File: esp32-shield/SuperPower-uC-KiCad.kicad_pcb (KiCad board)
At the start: 4 copper layers, 45.1 x 45.1 mm, 29 parts, among them J11 DNP, J5 Conn_01x14_Female, J6 Conn_01x14_Female, J9 MCU board, Q3 S8050, Q4 S8050, SW1 DNP, U13 ESP32-WROOM32, U14 W25Q32JVSS, U5 CH340G, U6 AMS1117-3.3, Y1 12MHZ

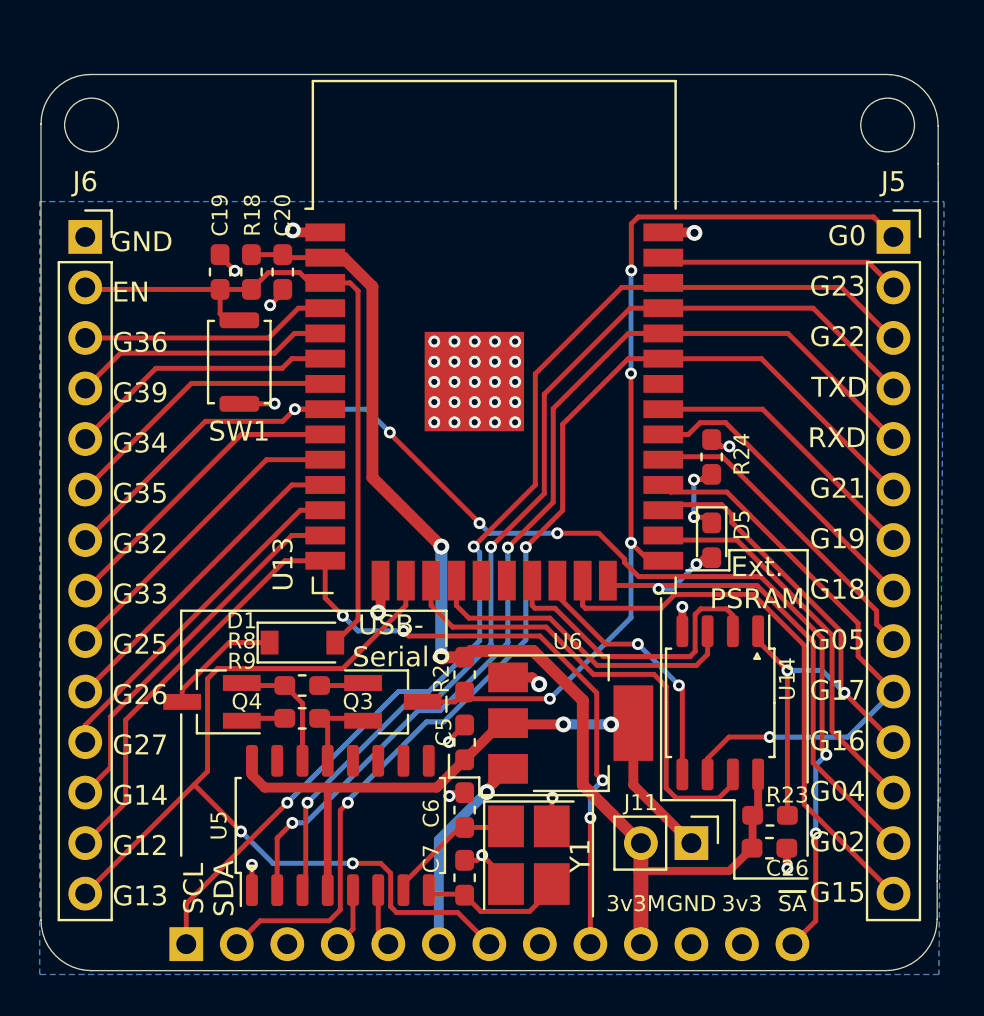
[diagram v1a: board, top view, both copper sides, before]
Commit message: added rgbw led, swapped ch340g for ch340c part numers
also marked crystal and caps as DNP
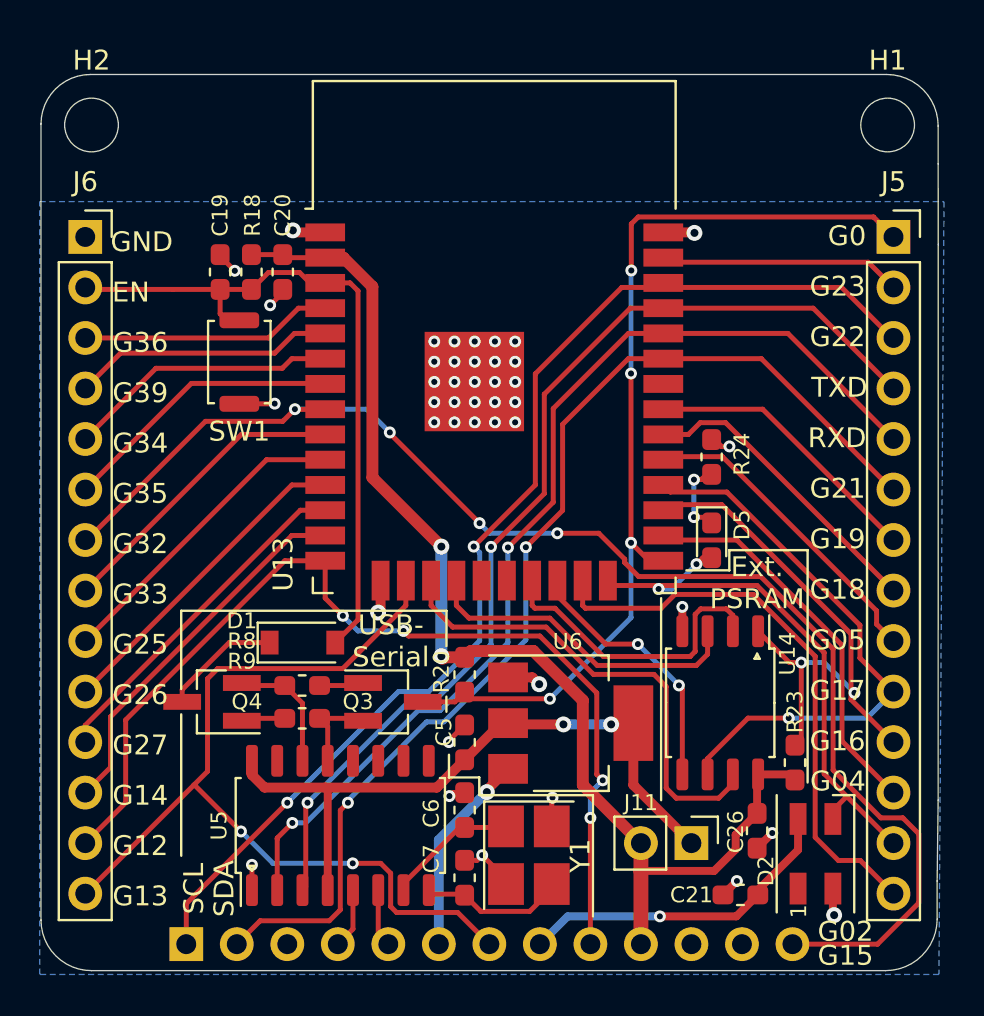
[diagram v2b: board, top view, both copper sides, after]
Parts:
- removed H4: MountingHole, MountingHole:MountingHole_2.7mm_M2.5_ISO7380
- added C21: 0.1µF, Capacitor_SMD:C_0603_1608Metric_Pad1.05x0.95mm_HandSolder, F.Cu at (161.1, 114.6)
- added D2: SK6812MINI, LED_SMD:LED_SK6812MINI_PLCC4_3.5x3.5mm_P1.75mm, F.Cu at (164.8, 112.5)
- added H1: MountingHole, MountingHole:MountingHole_2.7mm_M2.5_ISO7380, F.Cu at (168.5, 75.9)
- U5: value CH340G -> CH340C
- moved R23 2.94 mm to (163.8, 108.0), turned to 90 degrees
- moved C26 1.07 mm to (161.9, 111.4), turned to 90 degrees
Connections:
- net /3v3_MCU_2 renamed /3v3_MCU
- net /D2+ renamed /D+
- net /D2- renamed /D-
- net /SCL_2 renamed /SCL
- net /SDA_2 renamed /SDA
- net /VBUS_2 renamed /VBUS
- J9 pad 8: Net-(J9-Pad8) -> /5V
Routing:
- net /5V: track 0.00 -> 16.6 mm, vias 0 -> 1
- net /~SMBALERT: track 62.4 -> 69.4 mm, vias 6 -> 4
- net /MCU Module/IO16: track 31.8 -> 29.0 mm
- net GND: track 21.6 -> 23.9 mm, vias 40 -> 42
- net /3v3_MCU: track 58.5 -> 60.1 mm
- net /MCU Module/IO2: track 27.3 -> 28.7 mm
- net /MCU Module/IO15: track 28.1 -> 28.8 mm
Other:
- copper layers 4 -> 2
- board text removed: "3v3M"
- board text removed: "~SA"

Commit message: added more input caps & part number for button
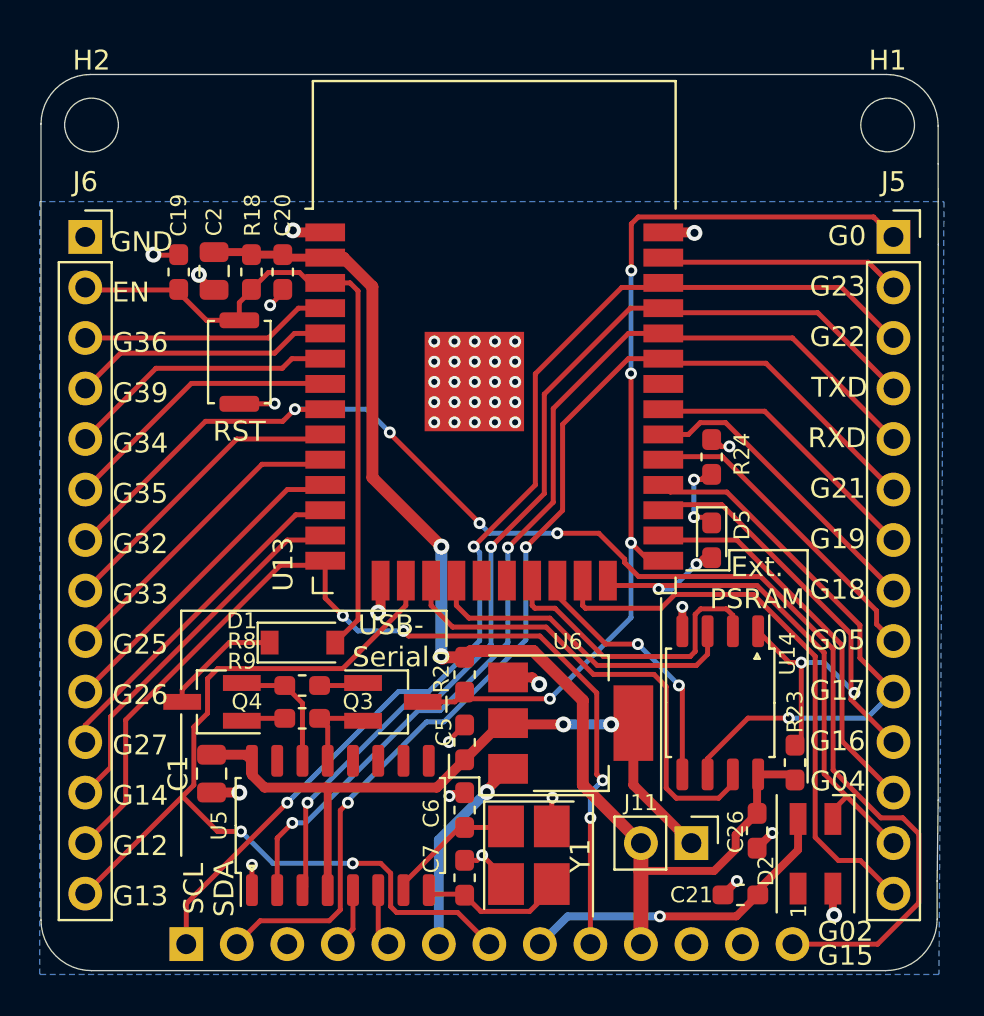
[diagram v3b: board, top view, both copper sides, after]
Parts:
- added C1: 22µF, Capacitor_SMD:C_0805_2012Metric, F.Cu at (134.5, 108.5)
- added C2: 22µF, Capacitor_SMD:C_0805_2012Metric, F.Cu at (134.6, 83.2)
- moved C19 2.08 mm to (132.8, 83.3)
- renumbered SW1 to RST
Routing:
- net GND: track 23.9 -> 26.5 mm, vias 42 -> 44
- net /MCU Module/3v3_UART: track 34.3 -> 36.4 mm
- net /3v3_MCU: track 60.1 -> 62.0 mm
